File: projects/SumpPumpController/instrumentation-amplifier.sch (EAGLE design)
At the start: 8 parts, among them CN1 1X4-BIG, U1 AD8293GARJZ-R7CT-ND

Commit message: Updated instrumentation schematic to include voltage divider on the reference pin
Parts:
- added R1, R2: 2k, adafruit:R-US_R0603
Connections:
- new net N$3: R1.2, R2.1, U1.REF
- net GND: now also R2.2
- net V+: now also R1.1
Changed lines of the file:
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@@
 <part name="P+3" library="supply1" deviceset="V+" device=""/>
 <part name="GND3" library="supply1" deviceset="GND" device=""/>
+<part name="P+4" library="supply1" deviceset="V+" device=""/>
+<part name="R1" library="adafruit" deviceset="R-US_" device="R0603" value="2k"/>
+<part name="R2" library="adafruit" deviceset="R-US_" device="R0603" value="2k"/>
 </parts>
 <sheets>
@@
 <instance part="CN1" gate="G$1" x="-30.48" y="15.24" rot="R180"/>
 <instance part="P+1" gate="1" x="53.34" y="40.64"/>
-<instance part="GND1" gate="1" x="66.04" y="-2.54"/>
+<instance part="GND1" gate="1" x="30.48" y="-7.62"/>
 <instance part="VCC" gate="G$1" x="73.66" y="30.48" rot="R180"/>
 <instance part="SIGNAL" gate="G$1" x="73.66" y="20.32" rot="R180"/>
@@
 <instance part="P+3" gate="1" x="-20.32" y="30.48"/>
 <instance part="GND3" gate="1" x="-20.32" y="2.54"/>
+<instance part="P+4" gate="1" x="0" y="-2.54" rot="R90"/>
+<instance part="R1" gate="G$1" x="10.16" y="-2.54"/>
+<instance part="R2" gate="G$1" x="25.4" y="-2.54"/>
 </instances>
 <busses>
@@
 <wire x1="66.04" y1="10.16" x2="66.04" y2="2.54" width="0.1524" layer="91"/>
 <pinref part="U1" gate="G$1" pin="-V"/>
-<wire x1="66.04" y1="2.54" x2="66.04" y2="0" width="0.1524" layer="91"/>
 <wire x1="12.7" y1="5.08" x2="12.7" y2="2.54" width="0.1524" layer="91"/>
 <pinref part="C2" gate="G$1" pin="1"/>
@@
 <wire x1="30.48" y1="2.54" x2="66.04" y2="2.54" width="0.1524" layer="91"/>
 <junction x="30.48" y="2.54"/>
-<junction x="66.04" y="2.54"/>
+<pinref part="R2" gate="G$1" pin="2"/>
+<wire x1="30.48" y1="2.54" x2="30.48" y2="-2.54" width="0.1524" layer="91"/>
+<wire x1="30.48" y1="-2.54" x2="30.48" y2="-5.08" width="0.1524" layer="91"/>
+<junction x="30.48" y="-2.54"/>
 </segment>
 <segment>
@@
 <wire x1="-20.32" y1="20.32" x2="-20.32" y2="27.94" width="0.1524" layer="91"/>
 </segment>
+<segment>
+<pinref part="R1" gate="G$1" pin="1"/>
+<pinref part="P+4" gate="1" pin="V+"/>
+<wire x1="2.54" y1="-2.54" x2="5.08" y2="-2.54" width="0.1524" layer="91"/>
+</segment>
 </net>
 <net name="N$6" class="0">
@@
 </segment>
 </net>
+<net name="N$3" class="0">
+<segment>
+<pinref part="R2" gate="G$1" pin="1"/>
+<pinref part="R1" gate="G$1" pin="2"/>
+<wire x1="20.32" y1="-2.54" x2="17.78" y2="-2.54" width="0.1524" layer="91"/>
+<pinref part="U1" gate="G$1" pin="REF"/>
+<wire x1="17.78" y1="-2.54" x2="15.24" y2="-2.54" width="0.1524" layer="91"/>
+<wire x1="17.78" y1="10.16" x2="17.78" y2="-2.54" width="0.1524" layer="91"/>
+<junction x="17.78" y="-2.54"/>
+</segment>
+</net>

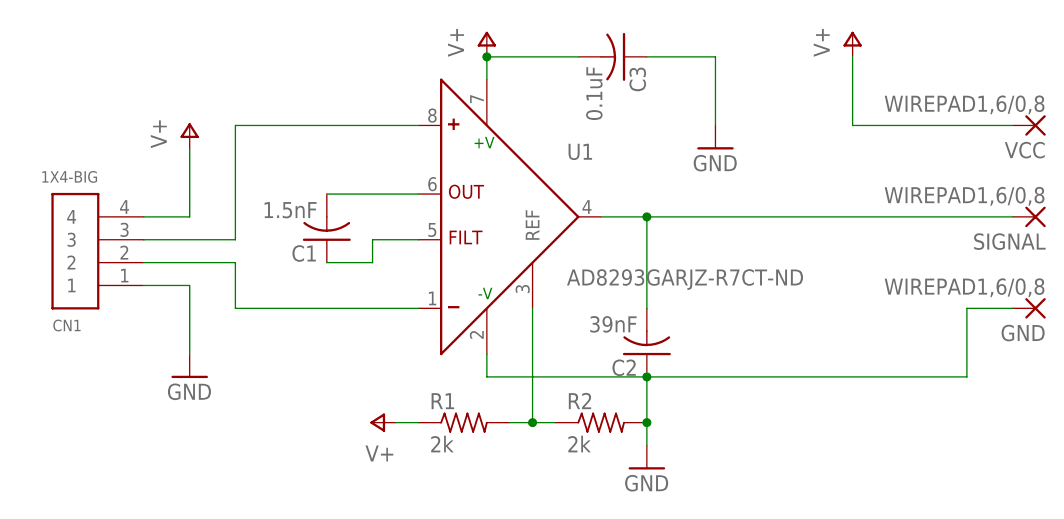
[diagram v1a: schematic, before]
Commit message: Added more debug output Adjusted instrumentation amplifier circuit to inlude ~1Hz filter, as turbulence in the sensor triggers false positives; Fixed a bug where self test time was not accounted for when delaying DC pump measurement;
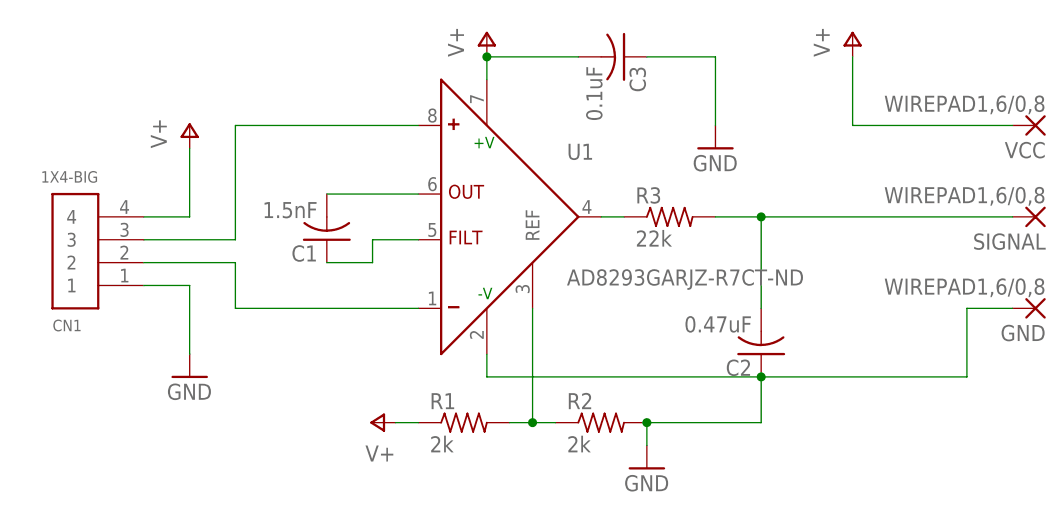
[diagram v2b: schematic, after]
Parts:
- added R3: 22k, adafruit:R-US_R0603
- C2: value 39nF -> 0.47uF
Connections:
- new net N$8: R3.1, U1.ADC-OUT
- net N$4: now also R3.2; no longer U1.ADC-OUT
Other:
- moved on the sheet: C2
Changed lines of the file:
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@@
 <part name="U1" library="serge" deviceset="AD8293G***ARJZ-R7CT-ND" device=""/>
 <part name="C1" library="adafruit" deviceset="C-US" device="025-024X044" value="1.5nF"/>
-<part name="C2" library="adafruit" deviceset="C-US" device="050-024X044" value="39nF"/>
+<part name="C2" library="adafruit" deviceset="C-US" device="050-024X044" value="0.47uF"/>
 <part name="C3" library="adafruit" deviceset="C-US" device="050-024X044" value="0.1uF"/>
 <part name="CN1" library="adafruit" deviceset="1X4" device="-BIG"/>
@@
 <part name="R1" library="adafruit" deviceset="R-US_" device="R0603" value="2k"/>
 <part name="R2" library="adafruit" deviceset="R-US_" device="R0603" value="2k"/>
+<part name="R3" library="adafruit" deviceset="R-US_" device="R0603" value="22k"/>
 </parts>
 <sheets>
@@
 <instance part="U1" gate="G$1" x="12.7" y="20.32"/>
 <instance part="C1" gate="G$1" x="-5.08" y="17.78" rot="R180"/>
-<instance part="C2" gate="G$1" x="30.48" y="5.08" rot="R180"/>
+<instance part="C2" gate="G$1" x="43.18" y="5.08" rot="R180"/>
 <instance part="C3" gate="G$1" x="27.94" y="38.1" rot="R270"/>
 <instance part="CN1" gate="G$1" x="-30.48" y="15.24" rot="R180"/>
@@
 <instance part="R1" gate="G$1" x="10.16" y="-2.54"/>
 <instance part="R2" gate="G$1" x="25.4" y="-2.54"/>
+<instance part="R3" gate="G$1" x="33.02" y="20.32"/>
 </instances>
 <busses>
@@
 <segment>
 <pinref part="C2" gate="G$1" pin="2"/>
-<wire x1="30.48" y1="10.16" x2="30.48" y2="20.32" width="0.1524" layer="91"/>
-<pinref part="U1" gate="G$1" pin="ADC-OUT"/>
-<wire x1="30.48" y1="20.32" x2="25.4" y2="20.32" width="0.1524" layer="91"/>
+<wire x1="43.18" y1="10.16" x2="43.18" y2="20.32" width="0.1524" layer="91"/>
 <pinref part="SIGNAL" gate="G$1" pin="P"/>
-<wire x1="71.12" y1="20.32" x2="30.48" y2="20.32" width="0.1524" layer="91"/>
-<junction x="30.48" y="20.32"/>
+<wire x1="71.12" y1="20.32" x2="43.18" y2="20.32" width="0.1524" layer="91"/>
+<pinref part="R3" gate="G$1" pin="2"/>
+<wire x1="43.18" y1="20.32" x2="38.1" y2="20.32" width="0.1524" layer="91"/>
+<junction x="43.18" y="20.32"/>
 </segment>
 </net>
@@
 <wire x1="12.7" y1="5.08" x2="12.7" y2="2.54" width="0.1524" layer="91"/>
 <pinref part="C2" gate="G$1" pin="1"/>
-<wire x1="12.7" y1="2.54" x2="30.48" y2="2.54" width="0.1524" layer="91"/>
-<wire x1="30.48" y1="2.54" x2="66.04" y2="2.54" width="0.1524" layer="91"/>
-<junction x="30.48" y="2.54"/>
+<wire x1="12.7" y1="2.54" x2="43.18" y2="2.54" width="0.1524" layer="91"/>
+<wire x1="43.18" y1="2.54" x2="66.04" y2="2.54" width="0.1524" layer="91"/>
+<junction x="43.18" y="2.54"/>
 <pinref part="R2" gate="G$1" pin="2"/>
-<wire x1="30.48" y1="2.54" x2="30.48" y2="-2.54" width="0.1524" layer="91"/>
 <wire x1="30.48" y1="-2.54" x2="30.48" y2="-5.08" width="0.1524" layer="91"/>
 <junction x="30.48" y="-2.54"/>
+<wire x1="30.48" y1="-2.54" x2="43.18" y2="-2.54" width="0.1524" layer="91"/>
+<wire x1="43.18" y1="-2.54" x2="43.18" y2="2.54" width="0.1524" layer="91"/>
 </segment>
 <segment>
@@
 </segment>
 </net>
+<net name="N$8" class="0">
+<segment>
+<pinref part="R3" gate="G$1" pin="1"/>
+<pinref part="U1" gate="G$1" pin="ADC-OUT"/>
+<wire x1="27.94" y1="20.32" x2="25.4" y2="20.32" width="0.1524" layer="91"/>
+</segment>
+</net>
